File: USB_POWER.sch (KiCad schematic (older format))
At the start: 26 parts

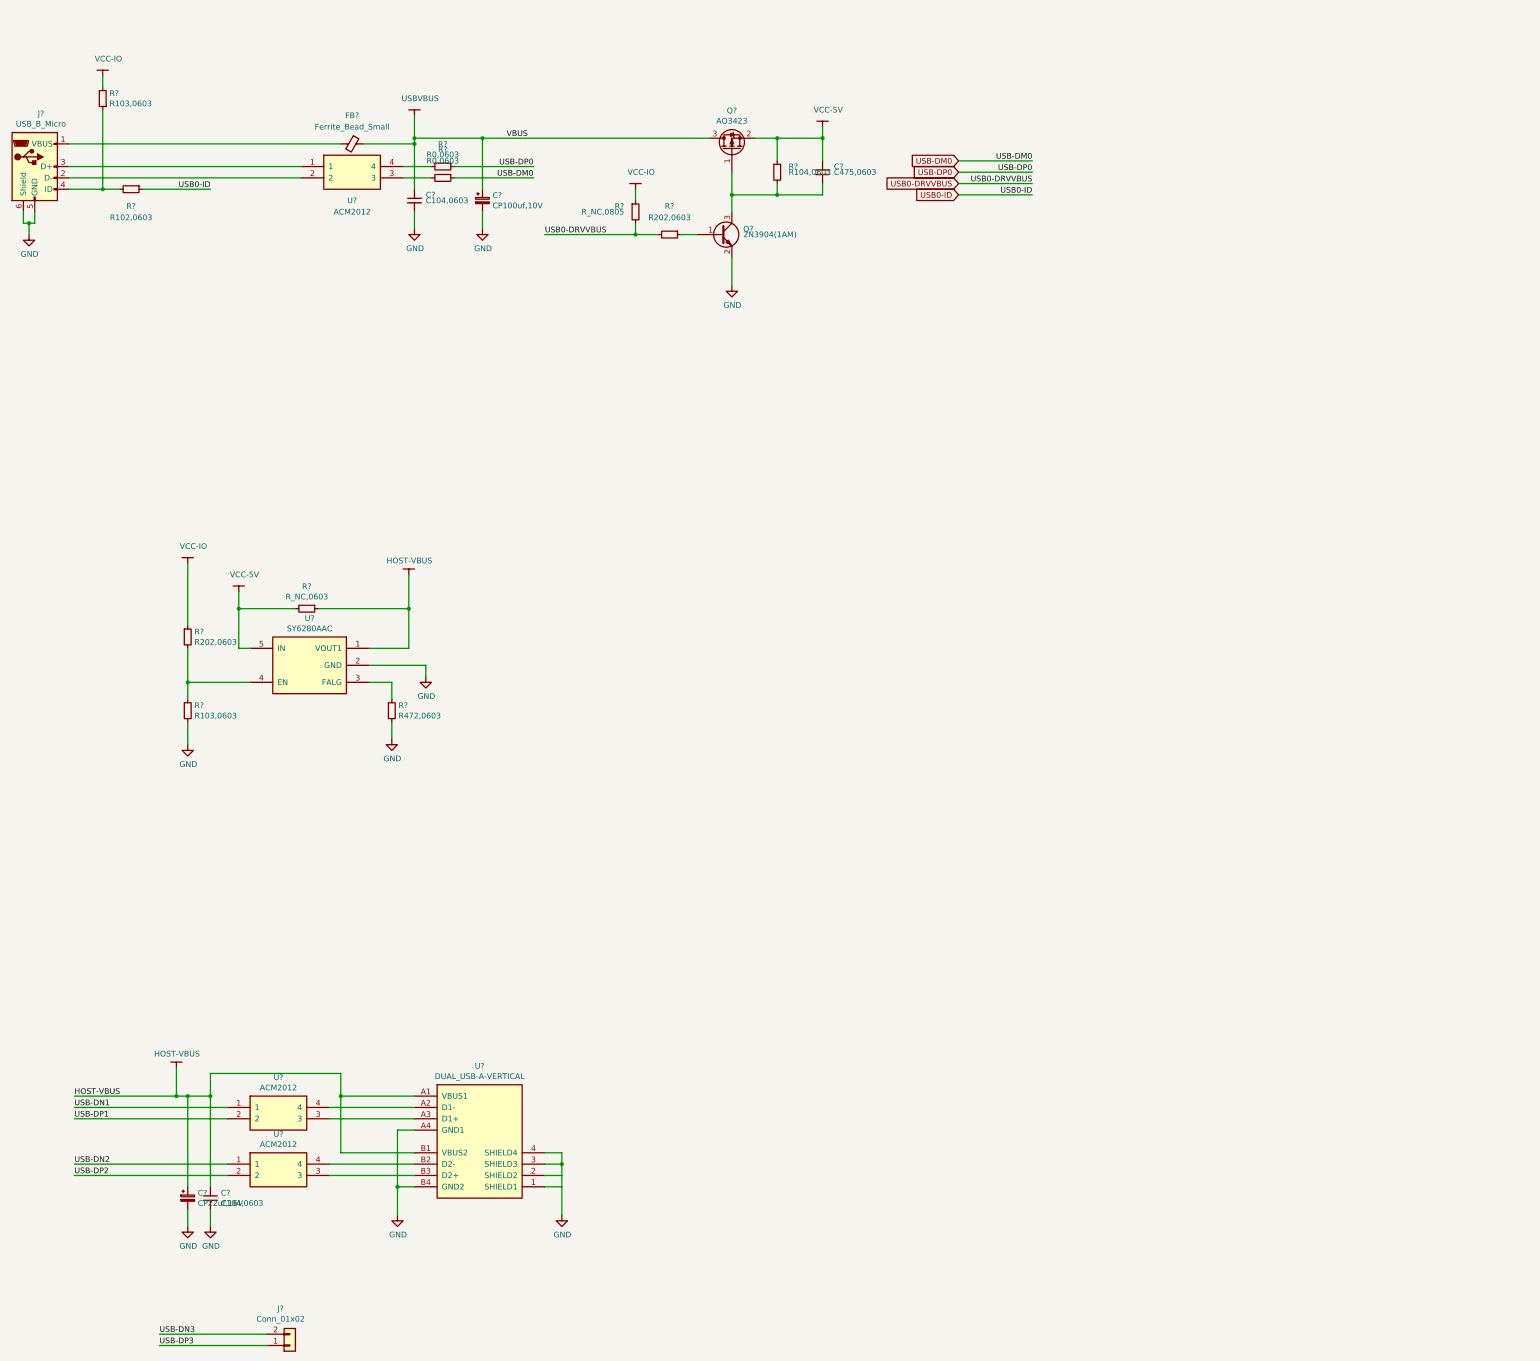
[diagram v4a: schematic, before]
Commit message: update USB schematic,
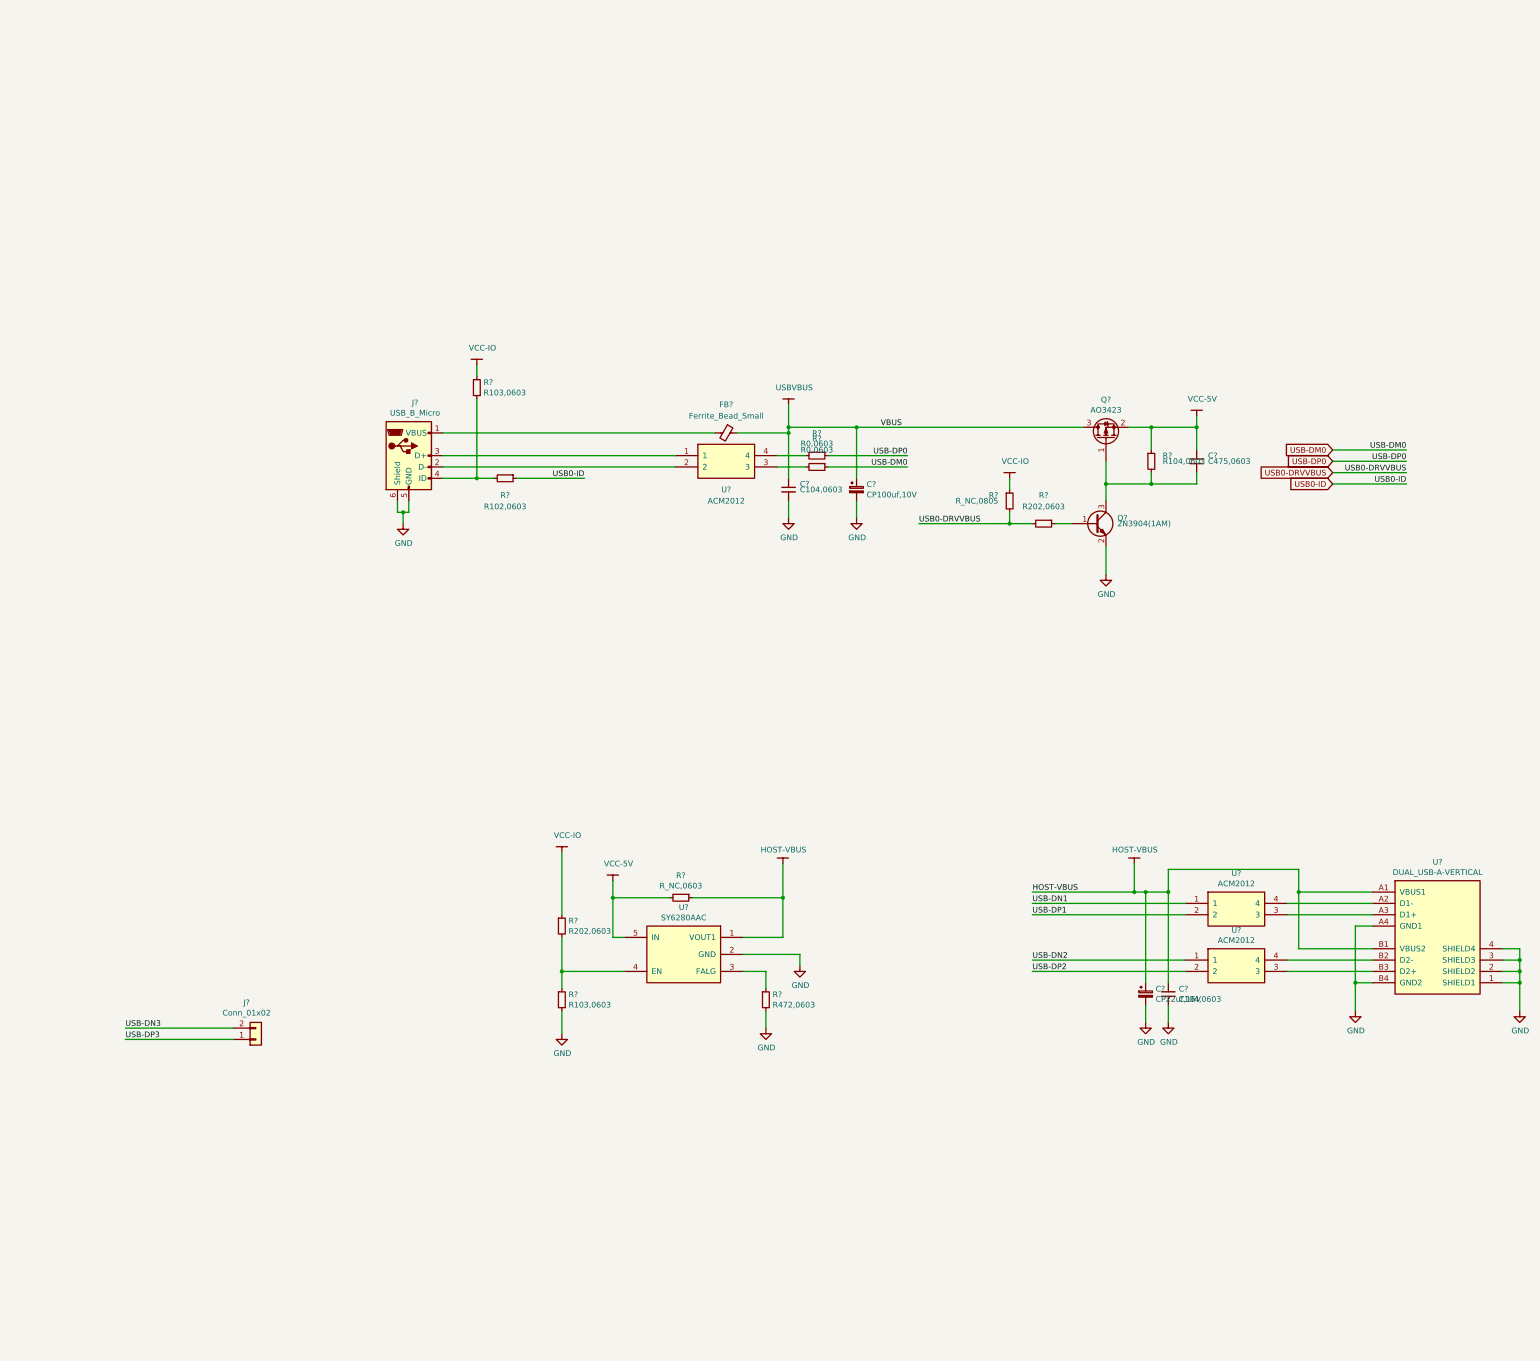
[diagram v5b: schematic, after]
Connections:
- net GND: now also U?.1 (SHIELD1), U?.2 (SHIELD2)
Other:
- moved on the sheet: C?, FB?, J?, Q?, R?, U?

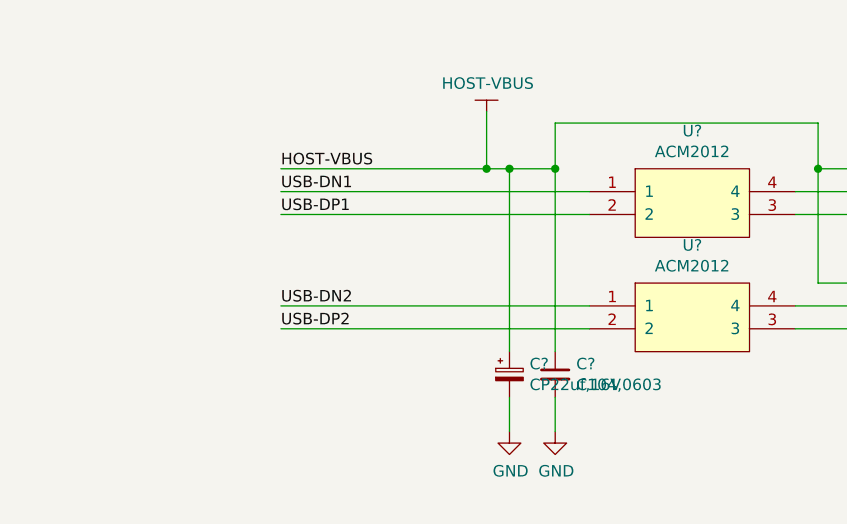
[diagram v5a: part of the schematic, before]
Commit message: update USB schematic,
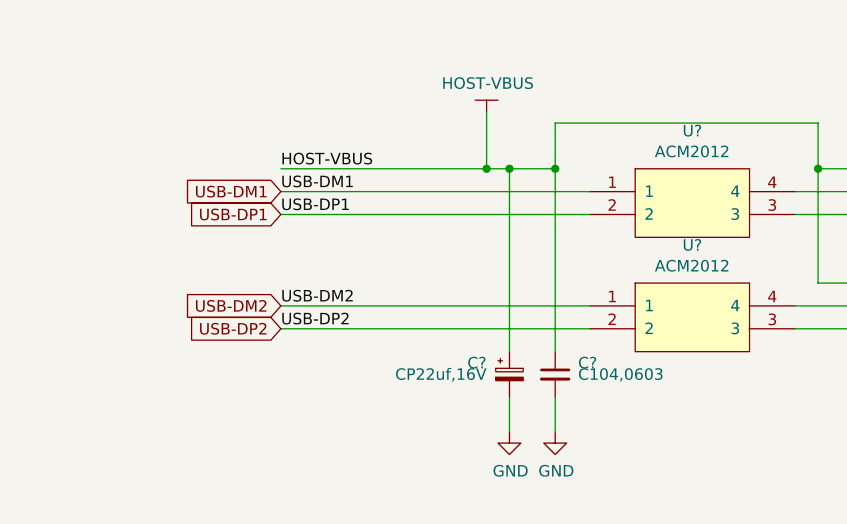
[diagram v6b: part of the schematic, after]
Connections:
- net USB-DN1 renamed USB-DM1
- net USB-DN2 renamed USB-DM2
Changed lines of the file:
@@
 $Descr A3 16535 11693
 encoding utf-8
-Sheet 12 34
+Sheet 11 33
 Title ""
 Date ""
@@
 AR Path="/5C22EE91/5C2E6048" Ref="C?"  Part="1"
 AR Path="/5C22DA43/5C2E6048" Ref="C?"  Part="1"
-F 0 "C?" H 11238 9096 50  0000 L CNN
-F 1 "CP22uf,16V" H 11238 9005 50  0000 L CNN
+F 0 "C?" H 11050 9100 50  0000 R CNN
+F 1 "CP22uf,16V" H 11050 9050 50  0000 R CNN
 F 2 "Capacitor_SMD:CP_Elec_4x5.3" H 11150 9050 50  0001 C CNN
 F 3 "~" H 11150 9050 50  0001 C CNN
@@
 AR Path="/5C22EE91/5C2E63CD" Ref="C?"  Part="1"
 AR Path="/5C22DA43/5C2E63CD" Ref="C?"  Part="1"
-F 0 "C?" H 11442 9096 50  0000 L CNN
-F 1 "C104,0603" H 11442 9005 50  0000 L CNN
+F 0 "C?" H 11450 9100 50  0000 L CNN
+F 1 "C104,0603" H 11450 9050 50  0000 L CNN
 F 2 "Capacitor_SMD:C_0603_1608Metric_Pad1.05x0.95mm_HandSolder" H 11350 9050 50  0001 C CNN
 F 3 "~" H 11350 9050 50  0001 C CNN
@@
 	13150 8350 12400 8350
 Text Label 10150 8250 0    50   ~ 0
-USB-DN1
+USB-DM1
 Text Label 10150 8350 0    50   ~ 0
 USB-DP1
 Text Label 10150 8750 0    50   ~ 0
-USB-DN2
+USB-DM2
 Text Label 10150 8850 0    50   ~ 0
 USB-DP2
@@
 Wire Wire Line
 	14450 8950 14450 8850
+Text GLabel 10150 8250 0    50   Input ~ 0
+USB-DM1
+Text GLabel 10150 8350 0    50   Input ~ 0
+USB-DP1
+Text GLabel 10150 8750 0    50   Input ~ 0
+USB-DM2
+Text GLabel 10150 8850 0    50   Input ~ 0
+USB-DP2
 $EndSCHEMATC
